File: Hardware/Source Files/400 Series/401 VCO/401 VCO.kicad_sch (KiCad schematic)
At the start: 0 parts

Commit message: wip on 401 oscillator. Core started
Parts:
- added C1: 180pF, 0_synthesis_smt:C_0603_1608Metric, symbol 0_synthesis_passives:CAP_180PF_0603_C0G
- added C2: 4.7nF, 0_synthesis_smt:C_0603_1608Metric, symbol 0_synthesis_passives:CAP_4.7NF_0603_C0G
- added C3, C4: 100nF, 0_synthesis_smt:C_0603_1608Metric, symbol 0_synthesis_passives:CAP_100NF_0603_X7R
- added C5: 20pF, 0_synthesis_smt:C_0603_1608Metric, symbol 0_synthesis_passives:CAP_20PF_0603_C0G
- added D1: 1N4148, Diode_SMD:D_SOD-323, symbol 0_synthesis_ic:DIODE_1N4148WS
- added Q1: DMMT3904W-7-F, Package_TO_SOT_SMD:SOT-363_SC-70-6, symbol 0_synthesis_ic:XSTR_MATCHED_PAIR_DMMT3904W-7-F
- added R1, R4: 2.2k, 0_synthesis_smt:R_0603_1608Metric, symbol 0_synthesis_passives:RES_2.2K_0603
- added R2, R5: 1Meg, 0_synthesis_smt:R_0603_1608Metric, symbol 0_synthesis_passives:RES_1MEG_0603
- added R3, R6, R8: 10k, 0_synthesis_smt:R_0603_1608Metric, symbol 0_synthesis_passives:RES_10k_0603
- added R7: 100k, 0_synthesis_smt:R_0603_1608Metric, symbol 0_synthesis_passives:RES_100k_0603
- added U1: TL074CPWR, 0_synthesis_smt:TSSOP-14_4.4x5mm_P0.65mm, symbol 0_synthesis_ic:TL074CPWR
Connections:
- new net: C2.2, R6.1, U1.8
- new net: C5.1, R5.1, R6.2, U1.13 (-)
- new net: C5.2, D1.2 (A), R5.2, U1.14
- new net: C1.2, R1.2, U1.1
- new net: C1.1, Q1.3 (C1), R2.2, U1.2 (-)
- new net: D1.1 (K), R7.2
- new net: R3.2, R4.2, U1.12 (+)
- new net: C2.1, Q1.6 (C2), U1.9 (-)
- new net: R7.1, R8.2
- new net: Q1.4 (E1), Q1.5 (E2), R1.1
- new net +12V: C3.1, R3.1, U1.4 (V+)
- new net -12V: C4.2, U1.11 (V-)
- new net GND: C3.2, C4.1, Q1.1 (B2), R4.1, R8.1, U1.10 (+), U1.3 (+)

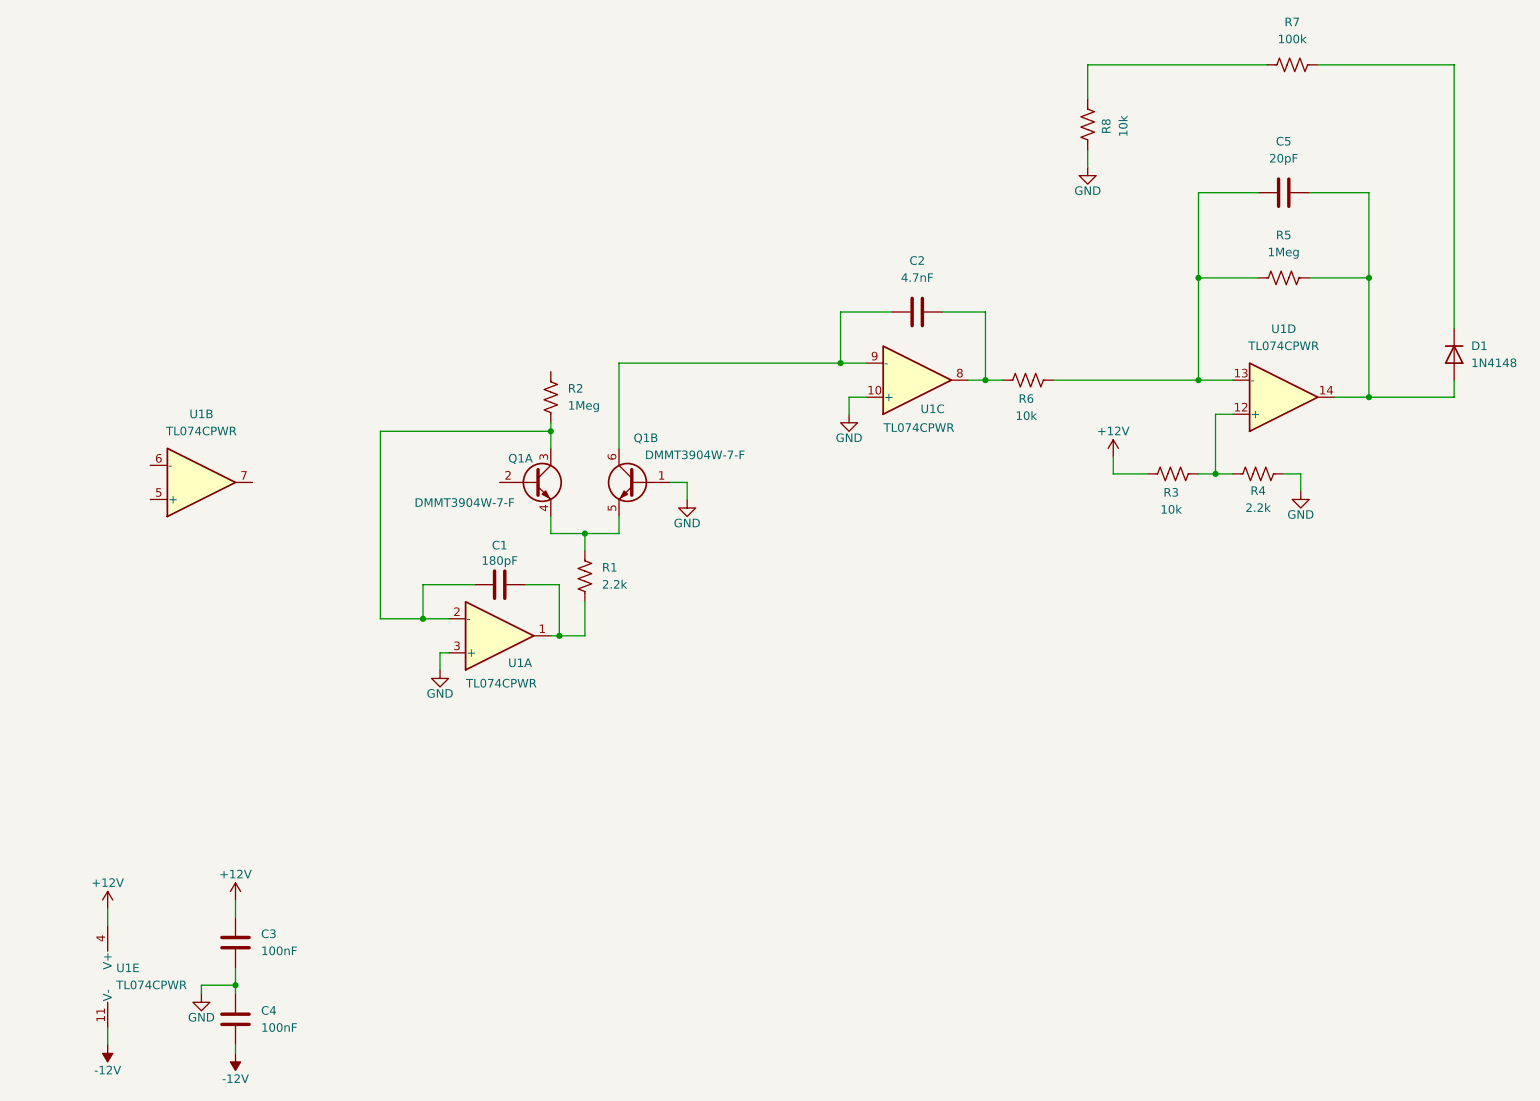
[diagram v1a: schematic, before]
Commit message: first pass of 401 VCO schematic
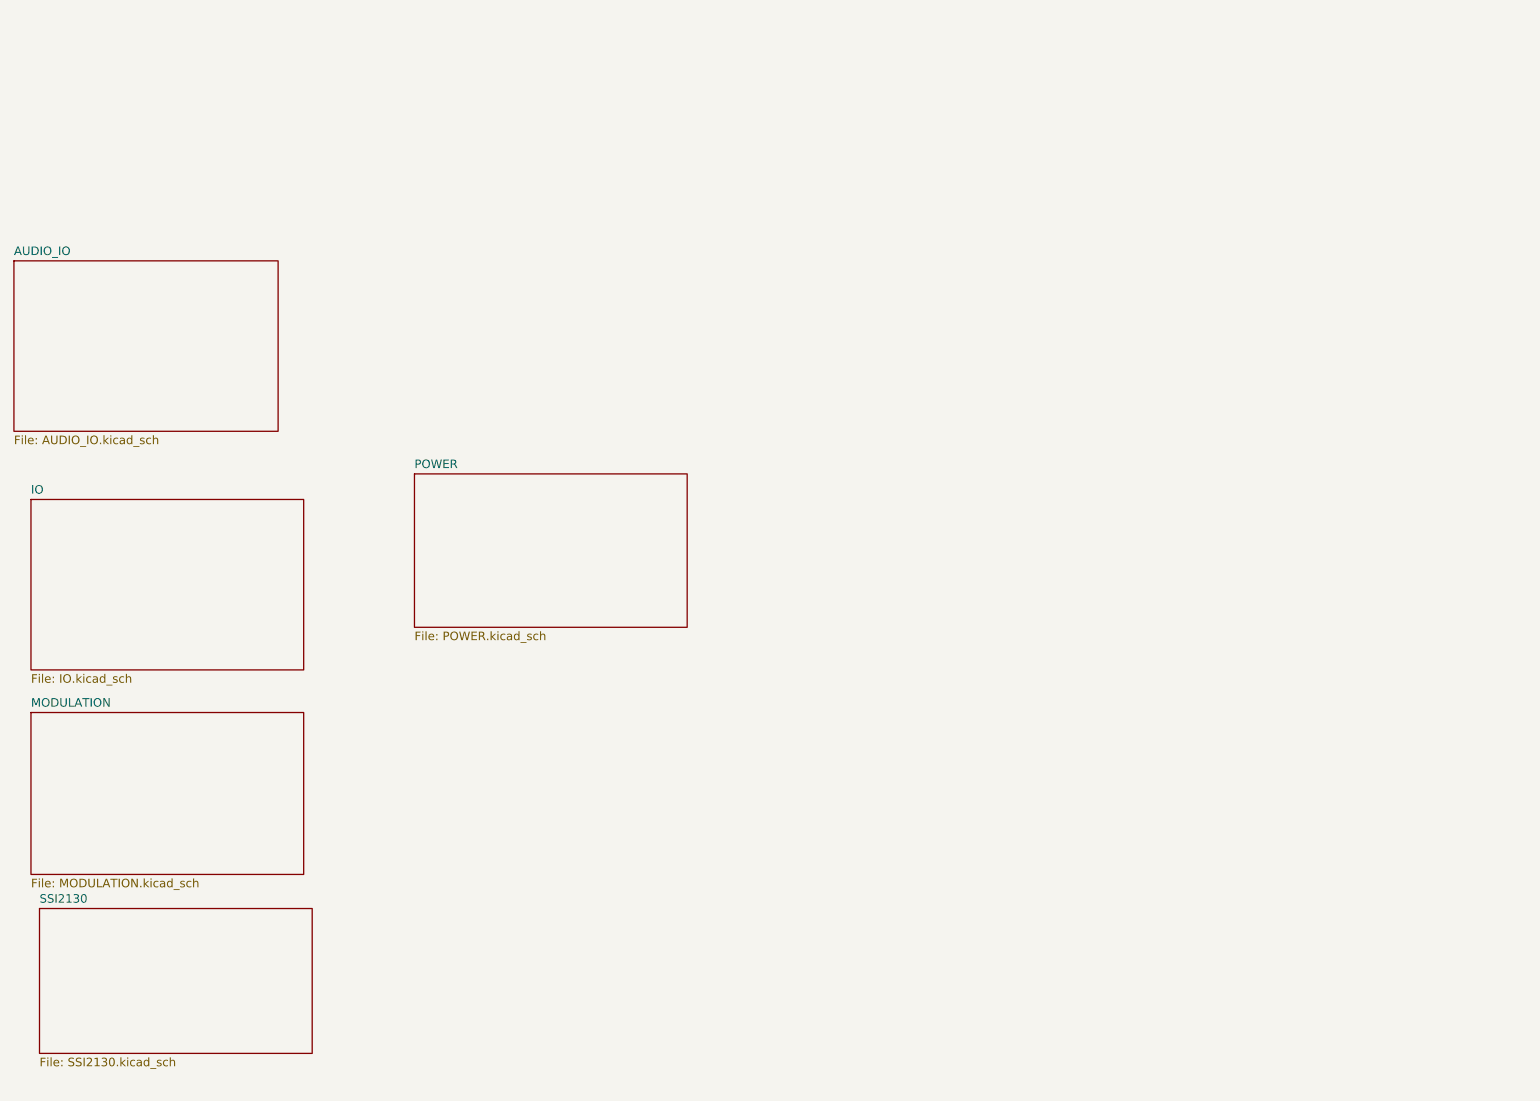
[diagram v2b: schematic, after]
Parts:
- removed C1: 180pF, 0_synthesis_smt:C_0603_1608Metric, symbol 0_synthesis_passives:CAP_180PF_0603_C0G
- removed C2: 4.7nF, 0_synthesis_smt:C_0603_1608Metric, symbol 0_synthesis_passives:CAP_4.7NF_0603_C0G
- removed C3, C4: 100nF, 0_synthesis_smt:C_0603_1608Metric, symbol 0_synthesis_passives:CAP_100NF_0603_X7R
- removed C5: 20pF, 0_synthesis_smt:C_0603_1608Metric, symbol 0_synthesis_passives:CAP_20PF_0603_C0G
- removed D1: 1N4148, Diode_SMD:D_SOD-323, symbol 0_synthesis_ic:DIODE_1N4148WS
- removed Q1: DMMT3904W-7-F, Package_TO_SOT_SMD:SOT-363_SC-70-6, symbol 0_synthesis_ic:XSTR_MATCHED_PAIR_DMMT3904W-7-F
- removed R1, R4: 2.2k, 0_synthesis_smt:R_0603_1608Metric, symbol 0_synthesis_passives:RES_2.2K_0603
- removed R2, R5: 1Meg, 0_synthesis_smt:R_0603_1608Metric, symbol 0_synthesis_passives:RES_1MEG_0603
- removed R3, R6, R8: 10k, 0_synthesis_smt:R_0603_1608Metric, symbol 0_synthesis_passives:RES_10k_0603
- removed R7: 100k, 0_synthesis_smt:R_0603_1608Metric, symbol 0_synthesis_passives:RES_100k_0603
- removed U1: TL074CPWR, 0_synthesis_smt:TSSOP-14_4.4x5mm_P0.65mm, symbol 0_synthesis_ic:TL074CPWR
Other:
- added sheet AUDIO_IO (AUDIO_IO.kicad_sch)
- added sheet IO (IO.kicad_sch)
- added sheet MODULATION (MODULATION.kicad_sch)
- added sheet POWER (POWER.kicad_sch)
- added sheet SSI2130 (SSI2130.kicad_sch)
